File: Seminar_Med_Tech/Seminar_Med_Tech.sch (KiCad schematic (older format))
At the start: 74 parts, among them J1 CONN_02X08, J7 CONN_02X08, U1 OPA132, U18 ADS1298, U20 ADS1298

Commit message: hi
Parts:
- TP1, TP2, TP3, TP4, TP5, TP6: footprint Measurement_Points:Test_Point_Keystone_5000-5004_Miniature -> Measurement_Points:Measurement_Point_Round-SMD-Pad_Small
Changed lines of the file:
@@
 F 0 "TP2" H 7500 6450 50  0000 C BNN
 F 1 "TEST" H 7500 6400 50  0000 C CNN
-F 2 "Measurement_Points:Test_Point_Keystone_5000-5004_Miniature" H 7500 6150 50  0001 C CNN
+F 2 "Measurement_Points:Measurement_Point_Round-SMD-Pad_Small" H 7500 6150 50  0001 C CNN
 F 3 "" H 7500 6150 50  0001 C CNN
 	1    7500 6150
@@
 F 0 "TP1" H 1200 5900 50  0000 C BNN
 F 1 "TEST" H 1200 5850 50  0000 C CNN
-F 2 "Measurement_Points:Test_Point_Keystone_5000-5004_Miniature" H 1200 5600 50  0001 C CNN
+F 2 "Measurement_Points:Measurement_Point_Round-SMD-Pad_Small" H 1200 5600 50  0001 C CNN
 F 3 "" H 1200 5600 50  0001 C CNN
 	1    1200 5600
@@
 F 0 "TP3" H 10525 6450 50  0000 C BNN
 F 1 "TEST" H 10525 6400 50  0000 C CNN
-F 2 "Measurement_Points:Test_Point_Keystone_5000-5004_Miniature" H 10525 6150 50  0001 C CNN
+F 2 "Measurement_Points:Measurement_Point_Round-SMD-Pad_Small" H 10525 6150 50  0001 C CNN
 F 3 "" H 10525 6150 50  0001 C CNN
 	1    10525 6150
@@
 F 0 "TP4" H 10700 6450 50  0000 C BNN
 F 1 "TEST" H 10700 6400 50  0000 C CNN
-F 2 "Measurement_Points:Test_Point_Keystone_5000-5004_Miniature" H 10700 6150 50  0001 C CNN
+F 2 "Measurement_Points:Measurement_Point_Round-SMD-Pad_Small" H 10700 6150 50  0001 C CNN
 F 3 "" H 10700 6150 50  0001 C CNN
 	1    10700 6150
@@
 F 0 "TP5" H 10875 6450 50  0000 C BNN
 F 1 "TEST" H 10875 6400 50  0000 C CNN
-F 2 "Measurement_Points:Test_Point_Keystone_5000-5004_Miniature" H 10875 6150 50  0001 C CNN
+F 2 "Measurement_Points:Measurement_Point_Round-SMD-Pad_Small" H 10875 6150 50  0001 C CNN
 F 3 "" H 10875 6150 50  0001 C CNN
 	1    10875 6150
@@
 F 0 "TP6" H 11050 6450 50  0000 C BNN
 F 1 "TEST" H 11050 6400 50  0000 C CNN
-F 2 "Measurement_Points:Test_Point_Keystone_5000-5004_Miniature" H 11050 6150 50  0001 C CNN
+F 2 "Measurement_Points:Measurement_Point_Round-SMD-Pad_Small" H 11050 6150 50  0001 C CNN
 F 3 "" H 11050 6150 50  0001 C CNN
 	1    11050 6150

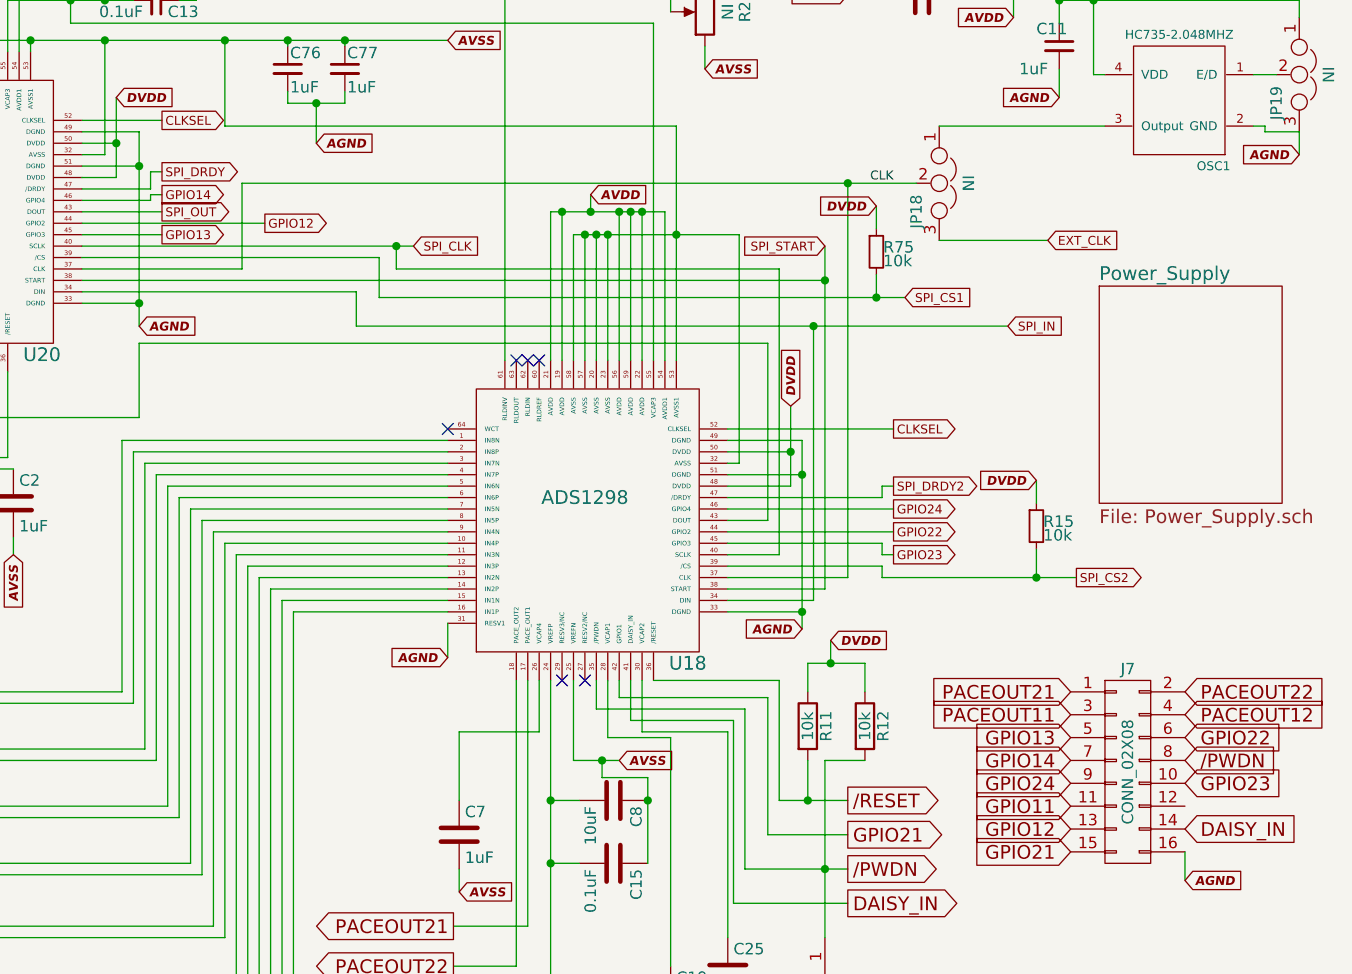
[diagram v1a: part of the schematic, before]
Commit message: Updated Connectors
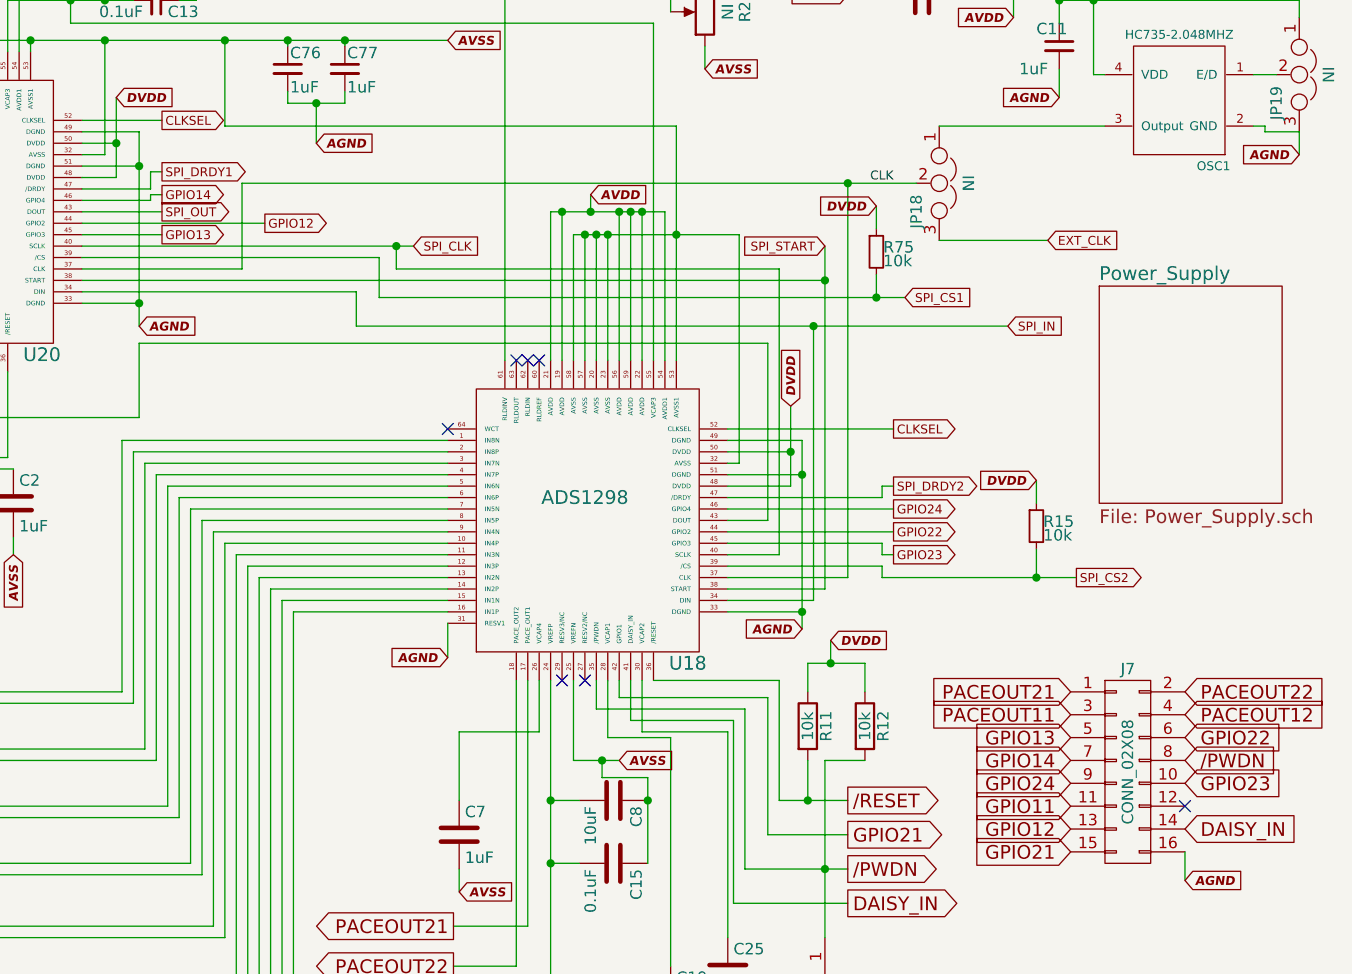
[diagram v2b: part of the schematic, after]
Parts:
- TP1, TP2, TP3, TP4, TP5, TP6: footprint Measurement_Points:Measurement_Point_Round-SMD-Pad_Small -> Measurement_Points:Test_Point_Keystone_5000-5004_Miniature
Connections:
- net SPI_DRDY renamed SPI_DRDY1
- no-connect marks 9 -> 10
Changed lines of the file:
@@
 F 0 "TP2" H 7500 6450 50  0000 C BNN
 F 1 "TEST" H 7500 6400 50  0000 C CNN
-F 2 "Measurement_Points:Measurement_Point_Round-SMD-Pad_Small" H 7500 6150 50  0001 C CNN
+F 2 "Measurement_Points:Test_Point_Keystone_5000-5004_Miniature" H 7500 6150 50  0001 C CNN
 F 3 "" H 7500 6150 50  0001 C CNN
 	1    7500 6150
@@
 F 0 "TP1" H 1200 5900 50  0000 C BNN
 F 1 "TEST" H 1200 5850 50  0000 C CNN
-F 2 "Measurement_Points:Measurement_Point_Round-SMD-Pad_Small" H 1200 5600 50  0001 C CNN
+F 2 "Measurement_Points:Test_Point_Keystone_5000-5004_Miniature" H 1200 5600 50  0001 C CNN
 F 3 "" H 1200 5600 50  0001 C CNN
 	1    1200 5600
@@
 F 0 "TP3" H 10525 6450 50  0000 C BNN
 F 1 "TEST" H 10525 6400 50  0000 C CNN
-F 2 "Measurement_Points:Measurement_Point_Round-SMD-Pad_Small" H 10525 6150 50  0001 C CNN
+F 2 "Measurement_Points:Test_Point_Keystone_5000-5004_Miniature" H 10525 6150 50  0001 C CNN
 F 3 "" H 10525 6150 50  0001 C CNN
 	1    10525 6150
@@
 F 0 "TP4" H 10700 6450 50  0000 C BNN
 F 1 "TEST" H 10700 6400 50  0000 C CNN
-F 2 "Measurement_Points:Measurement_Point_Round-SMD-Pad_Small" H 10700 6150 50  0001 C CNN
+F 2 "Measurement_Points:Test_Point_Keystone_5000-5004_Miniature" H 10700 6150 50  0001 C CNN
 F 3 "" H 10700 6150 50  0001 C CNN
 	1    10700 6150
@@
 F 0 "TP5" H 10875 6450 50  0000 C BNN
 F 1 "TEST" H 10875 6400 50  0000 C CNN
-F 2 "Measurement_Points:Measurement_Point_Round-SMD-Pad_Small" H 10875 6150 50  0001 C CNN
+F 2 "Measurement_Points:Test_Point_Keystone_5000-5004_Miniature" H 10875 6150 50  0001 C CNN
 F 3 "" H 10875 6150 50  0001 C CNN
 	1    10875 6150
@@
 F 0 "TP6" H 11050 6450 50  0000 C BNN
 F 1 "TEST" H 11050 6400 50  0000 C CNN
-F 2 "Measurement_Points:Measurement_Point_Round-SMD-Pad_Small" H 11050 6150 50  0001 C CNN
+F 2 "Measurement_Points:Test_Point_Keystone_5000-5004_Miniature" H 11050 6150 50  0001 C CNN
 F 3 "" H 11050 6150 50  0001 C CNN
 	1    11050 6150
@@
 CLKSEL
 Text GLabel 6100 2250 2    39   Output ~ 0
-SPI_DRDY
+SPI_DRDY1
 Text GLabel 6100 2350 2    39   Output ~ 0
 GPIO14
@@
 GPIO22
 NoConn ~ 13900 5175
+NoConn ~ 10575 5025
 $EndSCHEMATC

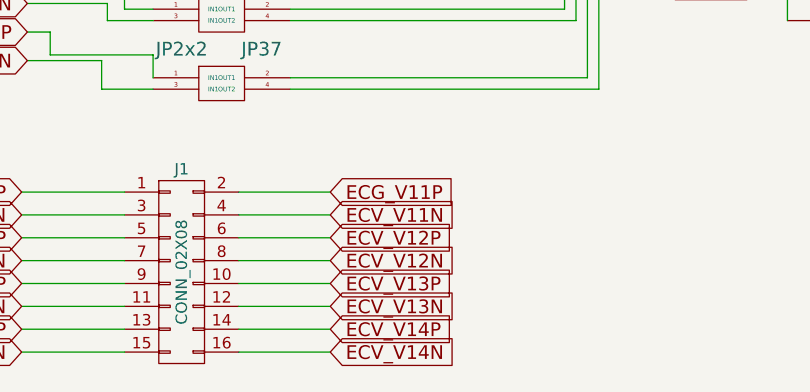
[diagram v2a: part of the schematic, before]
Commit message: Updated Schaltbild and added LM317 footprint
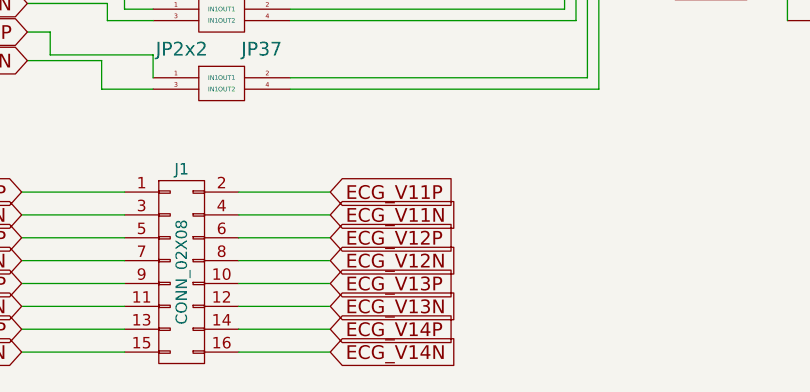
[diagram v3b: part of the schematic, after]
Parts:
- JP1, JP16, JP4, JP5: footprint jumper:Jumper1x2 -> Jumper:Jumper1x2
- JP17, JP18, JP19: footprint jumper:jumper1x3 -> Jumper:jumper1x3
- U1: footprint jumper:OPA132 -> Jumper:OPA132
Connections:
- net ECV_V11N: no longer J1.4 (P4)
- net ECV_V12N: no longer J1.8 (P8)
- net ECV_V12P: no longer J1.6 (P6)
- net ECV_V13N: no longer J1.12 (P12)
- net ECV_V13P: no longer J1.10 (P10)
- net ECV_V14N: no longer J1.16 (P16)
- net ECV_V14P: no longer J1.14 (P14)
- new net ECG_V11N: J1.4 (P4)
- new net ECG_V12N: J1.8 (P8)
- new net ECG_V12P: J1.6 (P6)
- new net ECG_V13N: J1.12 (P12)
- new net ECG_V13P: J1.10 (P10)
- new net ECG_V14N: J1.16 (P16)
- new net ECG_V14P: J1.14 (P14)
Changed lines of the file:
@@
 F 0 "JP16" H 3450 1325 50  0000 C CNN
 F 1 "Jumper" H 3450 1095 50  0000 C CNN
-F 2 "jumper:Jumper1x2" H 3450 1175 50  0001 C CNN
+F 2 "Jumper:Jumper1x2" H 3450 1175 50  0001 C CNN
 F 3 "" H 3450 1175 50  0001 C CNN
 	1    3450 1175
@@
 F 0 "JP5" H 9000 6050 50  0000 C CNN
 F 1 "Jumper" H 9000 5820 50  0000 C CNN
-F 2 "jumper:Jumper1x2" H 9000 5900 50  0001 C CNN
+F 2 "Jumper:Jumper1x2" H 9000 5900 50  0001 C CNN
 F 3 "" H 9000 5900 50  0001 C CNN
 	1    9000 5900
@@
 F 0 "JP4" H 2625 5500 50  0000 C CNN
 F 1 "Jumper" H 2625 5270 50  0000 C CNN
-F 2 "jumper:Jumper1x2" H 2625 5350 50  0001 C CNN
+F 2 "Jumper:Jumper1x2" H 2625 5350 50  0001 C CNN
 F 3 "" H 2625 5350 50  0001 C CNN
 	1    2625 5350
@@
 F 0 "JP17" H 6875 750 50  0000 L CNN
 F 1 "NI" H 6825 950 50  0000 C BNN
-F 2 "jumper:jumper1x3" H 6825 850 50  0001 C CNN
+F 2 "Jumper:jumper1x3" H 6825 850 50  0001 C CNN
 F 3 "" H 6825 850 50  0001 C CNN
 	1    6825 850
@@
 F 0 "JP1" H 4750 1375 50  0000 C CNN
 F 1 "Jumper" H 5000 1375 50  0000 C CNN
-F 2 "jumper:Jumper1x2" H 4875 1425 50  0001 C CNN
+F 2 "Jumper:Jumper1x2" H 4875 1425 50  0001 C CNN
 F 3 "" H 4875 1425 50  0001 C CNN
 	1    4875 1425
@@
 F 0 "JP18" H 9550 2200 50  0000 L CNN
 F 1 "NI" H 9500 2400 50  0000 C BNN
-F 2 "jumper:jumper1x3" H 9500 2300 50  0001 C CNN
+F 2 "Jumper:jumper1x3" H 9500 2300 50  0001 C CNN
 F 3 "" H 9500 2300 50  0001 C CNN
 	1    9500 2300
@@
 F 0 "JP19" H 11125 1725 50  0000 L CNN
 F 1 "NI" H 11075 1925 50  0000 C BNN
-F 2 "jumper:jumper1x3" H 11075 1825 50  0001 C CNN
+F 2 "Jumper:jumper1x3" H 11075 1825 50  0001 C CNN
 F 3 "" H 11075 1825 50  0001 C CNN
 	1    11075 1825
@@
 ECG_V11P
 Text GLabel 5500 7000 2    60   Input ~ 0
-ECV_V11N
+ECG_V11N
 Text GLabel 5500 7100 2    60   Input ~ 0
-ECV_V12P
+ECG_V12P
 Text GLabel 5500 7200 2    60   Input ~ 0
-ECV_V12N
+ECG_V12N
 Text GLabel 5500 7300 2    60   Input ~ 0
-ECV_V13P
+ECG_V13P
 Text GLabel 5500 7400 2    60   Input ~ 0
-ECV_V13N
+ECG_V13N
 Text GLabel 5500 7500 2    60   Input ~ 0
-ECV_V14P
+ECG_V14P
 Text GLabel 5500 7600 2    60   Input ~ 0
-ECV_V14N
+ECG_V14N
 Text Label 3050 1175 0    60   ~ 0
 WCT
@@
 F 0 "U1" H 10050 950 60  0000 C CNN
 F 1 "OPA132" H 10025 1300 60  0000 C CNN
-F 2 "jumper:OPA132" H 9925 1100 60  0001 C CNN
+F 2 "Jumper:OPA132" H 9925 1100 60  0001 C CNN
 F 3 "" H 9925 1100 60  0001 C CNN
 	1    9925 1100

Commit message: Update
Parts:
- J1: footprint Jumper:Jumper2x2 -> Pin_Headers:Pin_Header_Straight_2x08_Pitch2.54mm
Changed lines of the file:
@@
 F 0 "J1" H 4850 7700 50  0000 C CNN
 F 1 "CONN_02X08" V 4850 7250 50  0000 C CNN
-F 2 "Jumper:Jumper2x2" H 4850 6050 50  0001 C CNN
+F 2 "Pin_Headers:Pin_Header_Straight_2x08_Pitch2.54mm" H 4850 6050 50  0001 C CNN
 F 3 "" H 4850 6050 50  0001 C CNN
 	1    4850 7250

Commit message: Updates Schaltbild
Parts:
- added J?: CONN_02X08, symbol CONN_02X08
- TP1, TP2, TP3, TP4, TP5, TP6: footprint Measurement_Points:Test_Point_Keystone_5000-5004_Miniature -> Measurement_Points:Measurement_Point_Round-TH_Small
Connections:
- net ECG_V7N: now also JP23.2 (OUT1), U20.3 (IN7N), J?.5 (P5)
- net ECG_V7P: now also JP23.4 (OUT2), U20.4 (IN7P), J?.7 (P7)
- net ECG_V8N: now also JP22.2 (OUT1), U20.1 (IN8N), J?.1 (P1)
- net ECG_V8P: now also JP22.4 (OUT2), U20.2 (IN8P), J?.3 (P3)
- net ECG_V6N: now reaches JP24.2 (OUT1), U20.5 (IN6N)
- net ECG_V6N: now also J?.9 (P9)
- net ECG_V6P: now reaches JP24.4 (OUT2), U20.6 (IN6P)
- net ECG_V6P: now also J?.11 (P11)
- net ECG_V5N: now reaches JP25.2 (OUT1), U20.7 (IN5N)
- net ECG_V5N: now also J?.13 (P13)
- net ECG_V5P: now reaches JP25.4 (OUT2), U20.8 (IN5P)
- net ECG_V5P: now also J?.15 (P15)
- net ECG_V4N: now reaches JP26.2 (OUT1), U20.9 (IN4N)
- net ECG_V4N: now also J?.2 (P2)
- net ECG_V4P: now reaches JP26.4 (OUT2), U20.10 (IN4P)
- net ECG_V4P: now also J?.4 (P4)
- net ECG_V3N: now reaches JP27.2 (OUT1), U20.11 (IN3N)
- net ECG_V3N: now also J?.6 (P6)
- net ECG_V3P: now reaches JP27.4 (OUT2), U20.12 (IN3P)
- net ECG_V3P: now also J?.8 (P8)
- net ECG_V2N: now reaches JP28.2 (OUT1), U20.13 (IN2N)
- net ECG_V2N: now also J?.10 (P10)
- net ECG_V2P: now reaches JP28.4 (OUT2), U20.14 (IN2P)
- net ECG_V2P: now also J?.12 (P12)
- net ECG_V1N: now reaches JP29.2 (OUT1), U20.15 (IN1N)
- net ECG_V1N: now also J?.14 (P14)
- net ECG_V1P: now reaches JP29.4 (OUT2), U20.16 (IN1P)
- net ECG_V1P: now also J?.16 (P16)
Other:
- moved on the sheet: C90, JP16, JP22, JP23, JP24, JP25, JP26, JP27, JP28, JP29
